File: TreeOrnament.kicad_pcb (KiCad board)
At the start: 2 copper layers, 80 x 99 mm, 37 parts, among them J1 USB_B_Micro

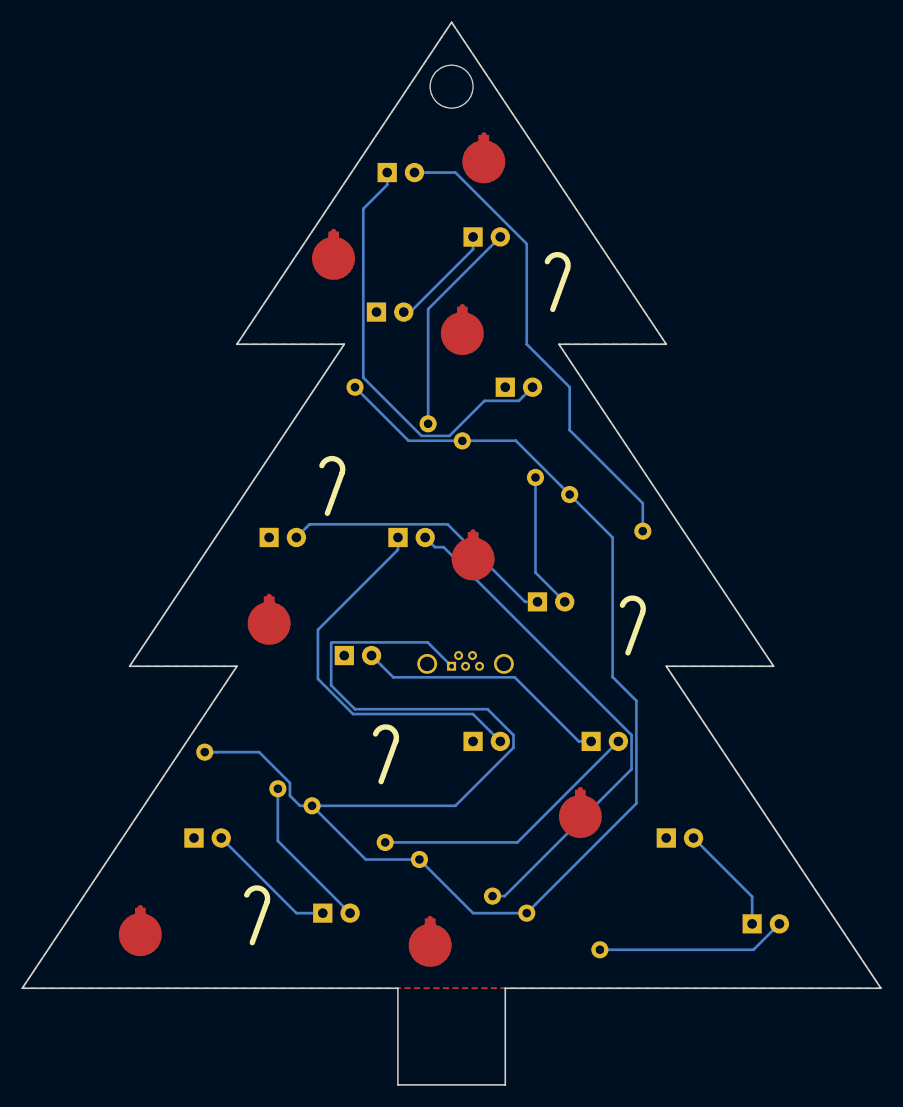
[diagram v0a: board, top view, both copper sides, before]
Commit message: Delete tracks.
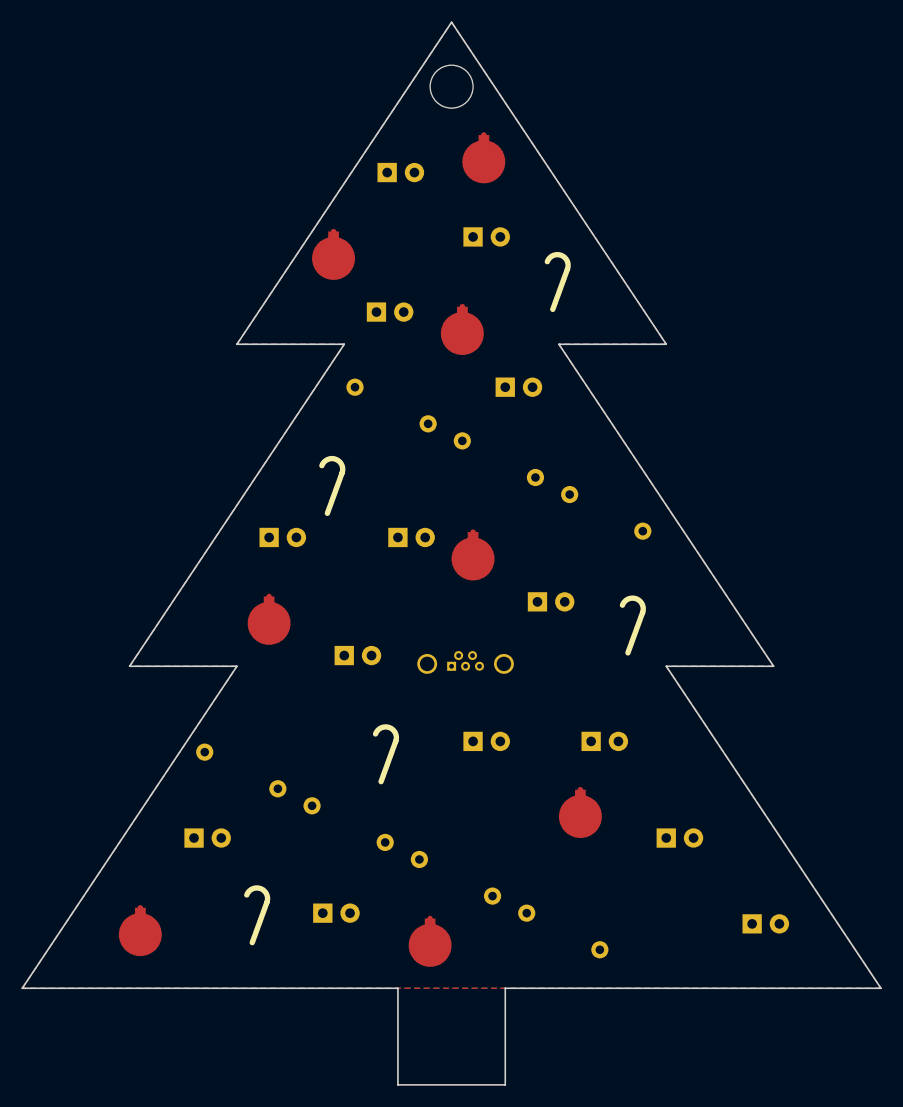
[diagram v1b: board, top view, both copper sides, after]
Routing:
- net +5V: track 164.1 -> 0.00 mm
- net Net-(D6-Pad2): track 47.9 -> 0.00 mm
- net Net-(D14-Pad2): track 44.5 -> 0.00 mm
- net Net-(D13-Pad2): track 39.9 -> 0.00 mm
- net Net-(D5-Pad2): track 35.7 -> 0.00 mm
- net Net-(D11-Pad2): track 26.0 -> 0.00 mm
- net Net-(D4-Pad2): track 25.6 -> 0.00 mm
- net Net-(D3-Pad2): track 23.8 -> 0.00 mm
- net Net-(D10-Pad2): track 20.2 -> 0.00 mm
- net Net-(D8-Pad2): track 17.7 -> 0.00 mm
- net Net-(D2-Pad2): track 14.4 -> 0.00 mm
- net Net-(D12-Pad2): track 12.7 -> 0.00 mm
- net Net-(D1-Pad2): track 12.4 -> 0.00 mm
- net Net-(D7-Pad2): track 10.3 -> 0.00 mm
- net Net-(D10-Pad1): track 10.0 -> 0.00 mm
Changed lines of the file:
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@@
   (general
     (links 30)
-    (no_connects 0)
+    (no_connects 30)
     (area 94.924999 29.924999 175.075001 131.075)
     (thickness 1.6)
     (drawings 17)
-    (tracks 87)
+    (tracks 0)
     (zones 0)
     (modules 37)
@@
   (gr_line (start 115 60) (end 125 60) (angle 90) (layer Edge.Cuts) (width 0.15))
   (gr_line (start 135 30) (end 115 60) (angle 90) (layer Edge.Cuts) (width 0.15))
-  (segment (start 123 113) (end 120.54 113) (width 0.25) (layer B.Cu) (net 2))
-  (segment (start 120.54 113) (end 113.54 106) (width 0.25) (layer B.Cu) (net 2))
-  (segment (start 118.813455 101.411924) (end 118.813455 106.273455) (width 0.25) (layer B.Cu) (net 3))
-  (segment (start 118.813455 106.273455) (end 125.54 113) (width 0.25) (layer B.Cu) (net 3))
-  (segment (start 148 97) (end 146.85 97) (width 0.25) (layer B.Cu) (net 4))
-  (segment (start 146.85 97) (end 140.880001 91.030001) (width 0.25) (layer B.Cu) (net 4))
-  (segment (start 140.880001 91.030001) (end 129.570001 91.030001) (width 0.25) (layer B.Cu) (net 4))
-  (segment (start 129.570001 91.030001) (end 128.439999 89.899999) (width 0.25) (layer B.Cu) (net 4))
-  (segment (start 128.439999 89.899999) (end 127.54 89) (width 0.25) (layer B.Cu) (net 4))
-  (segment (start 128.813455 106.411924) (end 141.128076 106.411924) (width 0.25) (layer B.Cu) (net 5))
-  (segment (start 141.128076 106.411924) (end 150.54 97) (width 0.25) (layer B.Cu) (net 5))
-  (segment (start 125.8136 94.450011) (end 136.990011 94.450011) (width 0.25) (layer B.Cu) (net 6))
-  (segment (start 122.549991 91.186401) (end 125.8136 94.450011) (width 0.25) (layer B.Cu) (net 6))
-  (segment (start 122.549991 86.600009) (end 122.549991 91.186401) (width 0.25) (layer B.Cu) (net 6))
-  (segment (start 136.990011 94.450011) (end 138.640001 96.100001) (width 0.25) (layer B.Cu) (net 6))
-  (segment (start 130 79.15) (end 122.549991 86.600009) (width 0.25) (layer B.Cu) (net 6))
-  (segment (start 130 78) (end 130 79.15) (width 0.25) (layer B.Cu) (net 6))
-  (segment (start 138.640001 96.100001) (end 139.54 97) (width 0.25) (layer B.Cu) (net 6))
-  (segment (start 138.813455 111.411924) (end 139.944825 111.411924) (width 0.25) (layer B.Cu) (net 7))
-  (segment (start 139.944825 111.411924) (end 151.765001 99.591748) (width 0.25) (layer B.Cu) (net 7))
-  (segment (start 151.765001 99.591748) (end 151.765001 96.411999) (width 0.25) (layer B.Cu) (net 7))
-  (segment (start 151.765001 96.411999) (end 134.253001 78.899999) (width 0.25) (layer B.Cu) (net 7))
-  (segment (start 134.253001 78.899999) (end 133.439999 78.899999) (width 0.25) (layer B.Cu) (net 7))
-  (segment (start 133.439999 78.899999) (end 132.54 78) (width 0.25) (layer B.Cu) (net 7))
-  (segment (start 163 114) (end 163 111.46) (width 0.25) (layer B.Cu) (net 8))
-  (segment (start 163 111.46) (end 157.54 106) (width 0.25) (layer B.Cu) (net 8))
-  (segment (start 148.813455 116.411924) (end 163.128076 116.411924) (width 0.25) (layer B.Cu) (net 9))
-  (segment (start 163.128076 116.411924) (end 165.54 114) (width 0.25) (layer B.Cu) (net 9))
-  (segment (start 126 94) (end 123.774999 91.774999) (width 0.25) (layer B.Cu) (net 10))
-  (segment (start 123.774999 91.774999) (end 123.774999 87.839999) (width 0.25) (layer B.Cu) (net 10))
-  (segment (start 123.774999 87.839999) (end 123.839999 87.774999) (width 0.25) (layer B.Cu) (net 10))
-  (segment (start 123.839999 87.774999) (end 132.774999 87.774999) (width 0.25) (layer B.Cu) (net 10))
-  (segment (start 132.774999 87.774999) (end 135 90) (width 0.25) (layer B.Cu) (net 10))
-  (segment (start 138.353002 94) (end 126 94) (width 0.25) (layer B.Cu) (net 10))
-  (segment (start 122 103) (end 135.353002 103) (width 0.25) (layer B.Cu) (net 10))
-  (segment (start 135.353002 103) (end 140.765001 97.588001) (width 0.25) (layer B.Cu) (net 10))
-  (segment (start 140.765001 97.588001) (end 140.765001 96.411999) (width 0.25) (layer B.Cu) (net 10))
-  (segment (start 140.765001 96.411999) (end 138.353002 94) (width 0.25) (layer B.Cu) (net 10))
-  (segment (start 122 103) (end 120.86863 103) (width 0.25) (layer B.Cu) (net 10))
-  (segment (start 120.86863 103) (end 119.938456 102.069826) (width 0.25) (layer B.Cu) (net 10))
-  (segment (start 119.938456 102.069826) (end 119.938456 100.871923) (width 0.25) (layer B.Cu) (net 10))
-  (segment (start 119.938456 100.871923) (end 117.066533 98) (width 0.25) (layer B.Cu) (net 10))
-  (segment (start 117.066533 98) (end 113.13137 98) (width 0.25) (layer B.Cu) (net 10))
-  (segment (start 113.13137 98) (end 112 98) (width 0.25) (layer B.Cu) (net 10))
-  (segment (start 132 108) (end 127 108) (width 0.25) (layer B.Cu) (net 10))
-  (segment (start 127 108) (end 122 103) (width 0.25) (layer B.Cu) (net 10))
-  (segment (start 142 113) (end 137 113) (width 0.25) (layer B.Cu) (net 10))
-  (segment (start 137 113) (end 132 108) (width 0.25) (layer B.Cu) (net 10))
-  (segment (start 150 91) (end 152.215012 93.215012) (width 0.25) (layer B.Cu) (net 10))
-  (segment (start 152.215012 93.215012) (end 152.215012 102.784988) (width 0.25) (layer B.Cu) (net 10))
-  (segment (start 152.215012 102.784988) (end 142.799999 112.200001) (width 0.25) (layer B.Cu) (net 10))
-  (segment (start 142.799999 112.200001) (end 142 113) (width 0.25) (layer B.Cu) (net 10))
-  (segment (start 150 78) (end 150 91) (width 0.25) (layer B.Cu) (net 10))
-  (segment (start 146 74) (end 150 78) (width 0.25) (layer B.Cu) (net 10))
-  (segment (start 145.200001 73.200001) (end 146 74) (width 0.25) (layer B.Cu) (net 10))
-  (segment (start 126 64) (end 130.986936 68.986936) (width 0.25) (layer B.Cu) (net 10))
-  (segment (start 130.986936 68.986936) (end 140.986936 68.986936) (width 0.25) (layer B.Cu) (net 10))
-  (segment (start 140.986936 68.986936) (end 145.200001 73.200001) (width 0.25) (layer B.Cu) (net 10))
-  (segment (start 137 50) (end 137 51.15) (width 0.25) (layer B.Cu) (net 14))
-  (segment (start 137 51.15) (end 131.15 57) (width 0.25) (layer B.Cu) (net 14))
-  (segment (start 131.15 57) (end 130.54 57) (width 0.25) (layer B.Cu) (net 14))
-  (segment (start 132.813455 67.411924) (end 132.813455 56.726545) (width 0.25) (layer B.Cu) (net 15))
-  (segment (start 132.813455 56.726545) (end 139.54 50) (width 0.25) (layer B.Cu) (net 15))
-  (segment (start 143 84) (end 141.85 84) (width 0.25) (layer B.Cu) (net 16))
-  (segment (start 141.85 84) (end 134.624999 76.774999) (width 0.25) (layer B.Cu) (net 16))
-  (segment (start 134.624999 76.774999) (end 121.765001 76.774999) (width 0.25) (layer B.Cu) (net 16))
-  (segment (start 121.765001 76.774999) (end 121.439999 77.100001) (width 0.25) (layer B.Cu) (net 16))
-  (segment (start 121.439999 77.100001) (end 120.54 78) (width 0.25) (layer B.Cu) (net 16))
-  (segment (start 142.813455 72.411924) (end 142.813455 81.273455) (width 0.25) (layer B.Cu) (net 17))
-  (segment (start 142.813455 81.273455) (end 145.54 84) (width 0.25) (layer B.Cu) (net 17))
-  (segment (start 141.267208 65.272792) (end 141.640001 64.899999) (width 0.25) (layer B.Cu) (net 18))
-  (segment (start 138.062206 65.272792) (end 141.267208 65.272792) (width 0.25) (layer B.Cu) (net 18))
-  (segment (start 141.640001 64.899999) (end 142.54 64) (width 0.25) (layer B.Cu) (net 18))
-  (segment (start 134.798073 68.536925) (end 138.062206 65.272792) (width 0.25) (layer B.Cu) (net 18))
-  (segment (start 132.201927 68.536925) (end 134.798073 68.536925) (width 0.25) (layer B.Cu) (net 18))
-  (segment (start 126.774999 63.109997) (end 132.201927 68.536925) (width 0.25) (layer B.Cu) (net 18))
-  (segment (start 126.774999 47.375001) (end 126.774999 63.109997) (width 0.25) (layer B.Cu) (net 18))
-  (segment (start 129 45.15) (end 126.774999 47.375001) (width 0.25) (layer B.Cu) (net 18))
-  (segment (start 129 44) (end 129 45.15) (width 0.25) (layer B.Cu) (net 18))
-  (segment (start 142 60) (end 142 50.646998) (width 0.25) (layer B.Cu) (net 19))
-  (segment (start 142 50.646998) (end 135.353002 44) (width 0.25) (layer B.Cu) (net 19))
-  (segment (start 135.353002 44) (end 132.812792 44) (width 0.25) (layer B.Cu) (net 19))
-  (segment (start 132.812792 44) (end 131.54 44) (width 0.25) (layer B.Cu) (net 19))
-  (segment (start 146 64) (end 142 60) (width 0.25) (layer B.Cu) (net 19))
-  (segment (start 146 68) (end 146 64) (width 0.25) (layer B.Cu) (net 19))
-  (segment (start 152.813455 74.813455) (end 146 68) (width 0.25) (layer B.Cu) (net 19))
-  (segment (start 152.813455 77.411924) (end 152.813455 74.813455) (width 0.25) (layer B.Cu) (net 19))
   (zone (net 1) (net_name GND) (layer F.Cu) (hatch edge 0.508)
     (connect_pads (clearance 0.508))
     (min_thickness 0.254)
-    (fill yes (arc_segments 16) (thermal_gap 0.508) (thermal_bridge_width 0.508))
+    (fill (arc_segments 16) (thermal_gap 0.508) (thermal_bridge_width 0.508))
     (polygon
       (pts
@@
     (connect_pads (clearance 0.508))
     (min_thickness 0.254)
-    (fill yes (arc_segments 16) (thermal_gap 0.508) (thermal_bridge_width 0.508))
+    (fill (arc_segments 16) (thermal_gap 0.508) (thermal_bridge_width 0.508))
     (polygon
       (pts

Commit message: place new resistors
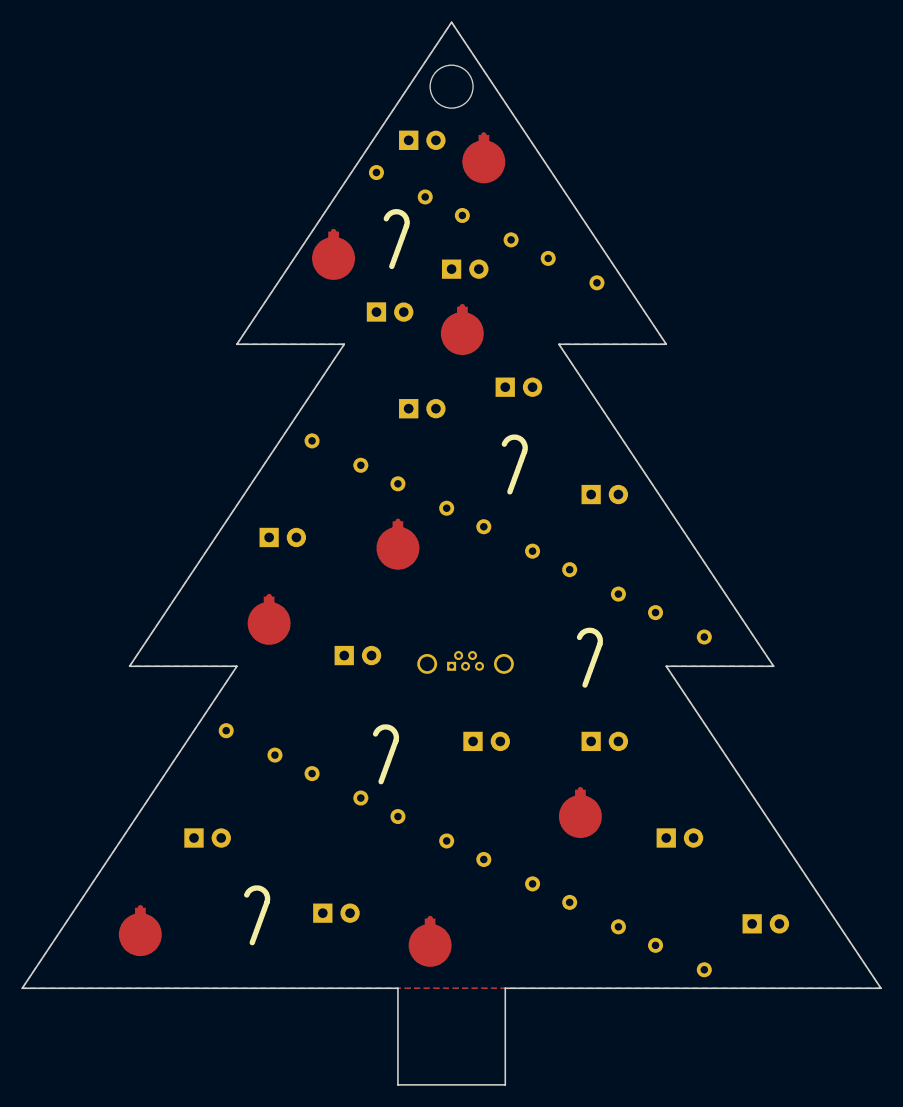
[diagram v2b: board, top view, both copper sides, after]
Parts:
- added R10: 56, myLibrary:R_Axial_DIN0204_L3.6mm_D1.6mm_P5.08mm_Horizontal, F.Cu at (146.0, 81.0)
- added R11: 56, myLibrary:R_Axial_DIN0204_L3.6mm_D1.6mm_P5.08mm_Horizontal, F.Cu at (154.0, 85.0)
- added R12: 56, myLibrary:R_Axial_DIN0204_L3.6mm_D1.6mm_P5.08mm_Horizontal, F.Cu at (128.0, 44.0)
- added R13: 56, myLibrary:R_Axial_DIN0204_L3.6mm_D1.6mm_P5.08mm_Horizontal, F.Cu at (136.0, 48.0)
- added R14: 56, myLibrary:R_Axial_DIN0204_L3.6mm_D1.6mm_P5.08mm_Horizontal, F.Cu at (144.0, 52.0)
- added R8: 56, myLibrary:R_Axial_DIN0204_L3.6mm_D1.6mm_P5.08mm_Horizontal, F.Cu at (130.0, 73.0)
- added R9: 56, myLibrary:R_Axial_DIN0204_L3.6mm_D1.6mm_P5.08mm_Horizontal, F.Cu at (138.0, 77.0)
- R1, R2, R3, R4, R5, R6, R7: footprint myLibrary:R_Axial_DIN0207_L6.3mm_D2.5mm_P7.62mm_Horizontal -> myLibrary:R_Axial_DIN0204_L3.6mm_D1.6mm_P5.08mm_Horizontal
- moved R5 52.0 mm to (146.0, 112.0)
- moved R6 50.3 mm to (154.0, 116.0)
- moved R7 24.5 mm to (122.0, 69.0)
- moved REF** 17.1 mm to (140.0, 72.0)
- moved REF** 15.5 mm to (129.0, 51.0)
- moved D6 12.0 mm to (131.0, 66.0)
- moved D12 11.2 mm to (148.0, 74.0)
- moved REF** 7.07 mm to (130.0, 79.0)
- moved R4 6.40 mm to (138.0, 108.0)
- moved REF** 5.00 mm to (147.0, 90.0)
- moved R3 4.47 mm to (130.0, 104.0)
- moved D10 3.61 mm to (135.0, 53.0)
- moved D14 3.61 mm to (131.0, 41.0)
- moved R2 3.00 mm to (122.0, 100.0)
- moved R1 2.83 mm to (114.0, 96.0)
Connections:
- D10 pad 1: Net-(D10-Pad1) -> GND
- D12 pad 1: Net-(D11-Pad2) -> GND
- D14 pad 1: Net-(D13-Pad2) -> GND
- D2 pad 1: Net-(D1-Pad2) -> GND
- D4 pad 1: Net-(D3-Pad2) -> GND
- D6 pad 1: Net-(D5-Pad2) -> GND
- D8 pad 1: Net-(D7-Pad2) -> GND
- D9 pad 2: Net-(D10-Pad1) -> Net-(D9-Pad2)
- R1 pad 2: Net-(D2-Pad2) -> Net-(D1-Pad2)
- R2 pad 2: Net-(D4-Pad2) -> Net-(D2-Pad2)
- R3 pad 2: Net-(D6-Pad2) -> Net-(D3-Pad2)
- R4 pad 2: Net-(D8-Pad2) -> Net-(D4-Pad2)
- R5 pad 2: Net-(D10-Pad2) -> Net-(D5-Pad2)
- R6 pad 2: Net-(D12-Pad2) -> Net-(D6-Pad2)
- R7 pad 2: Net-(D14-Pad2) -> Net-(D7-Pad2)

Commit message: remove year from silkscreen
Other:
- board text added: "Merry Christmas from Patrick Pelletier"
- board text removed: "Patrick Pelletier / Christmas 2017"
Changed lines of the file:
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@@
   (gr_line (start 140 129) (end 140 120) (angle 90) (layer Edge.Cuts) (width 0.15))
   (gr_line (start 130 120) (end 130 129) (angle 90) (layer Edge.Cuts) (width 0.15))
-  (gr_text "Patrick Pelletier / Christmas 2017" (at 136 104 333.4) (layer B.SilkS)
+  (gr_text "Merry Christmas from Patrick Pelletier" (at 122 117) (layer B.SilkS)
     (effects (font (size 1.5 1.5) (thickness 0.3)) (justify mirror))
   )
